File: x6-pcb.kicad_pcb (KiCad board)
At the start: 2 copper layers, 57.2 x 57.9 mm, 28 parts, among them SW1 SW_Push, U1 ATmega32U4-AU, Y1 16MHz

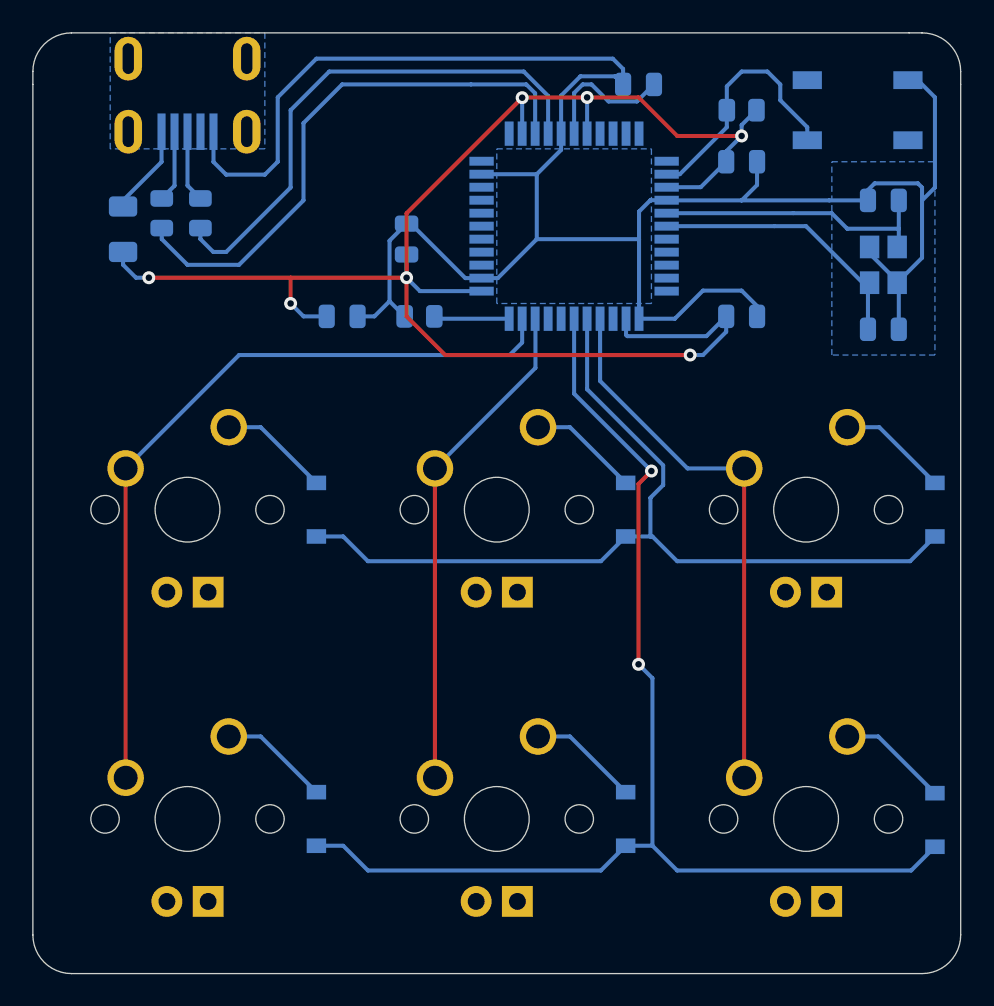
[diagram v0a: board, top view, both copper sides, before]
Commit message: Removed switch LEDs
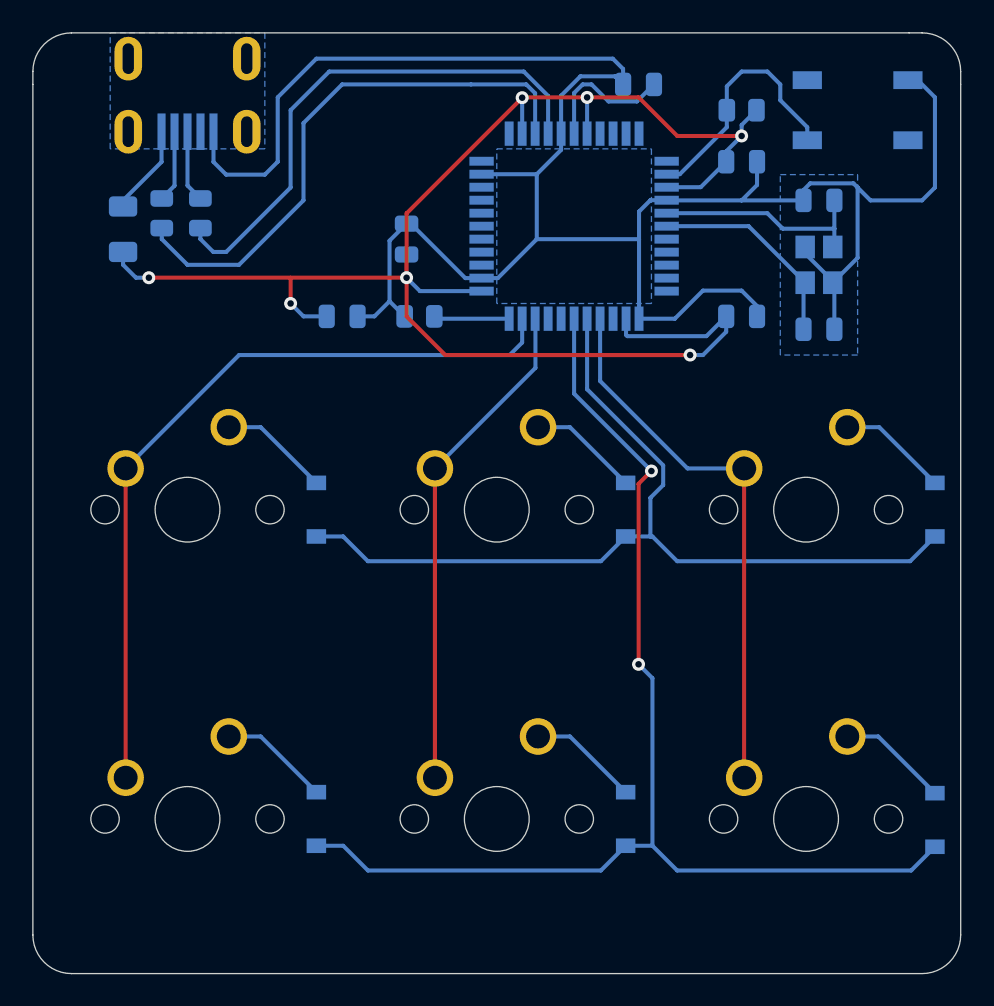
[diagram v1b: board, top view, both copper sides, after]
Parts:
- MX1, MX2, MX3, MX4, MX5, MX6: footprint MX_Only:MXOnly-1U -> MX_Only:MXOnly-1U-NoLED
- moved C1 3.97 mm to (178.6, 94.5)
- moved C2 3.97 mm to (178.6, 86.5)
- moved Y1 3.97 mm to (178.6, 90.5)
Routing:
- net Net-(C2-Pad1): track 17.6 -> 13.6 mm
- net Net-(C1-Pad1): track 16.9 -> 13.3 mm
